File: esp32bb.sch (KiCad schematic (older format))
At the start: 31 parts, among them CON1 Micro_SD_Card, IC1 FT232RQ, J1 CONN_01X18, P1 CONN_01X17, P3 USB_OTG, Q1 MMBT3904, Q2 MMBT3904, SW1 SWITCH_SPST, SW2 SWITCH_SPST, U1 ESP32-WROOM, U2 NJU7223DL1-33

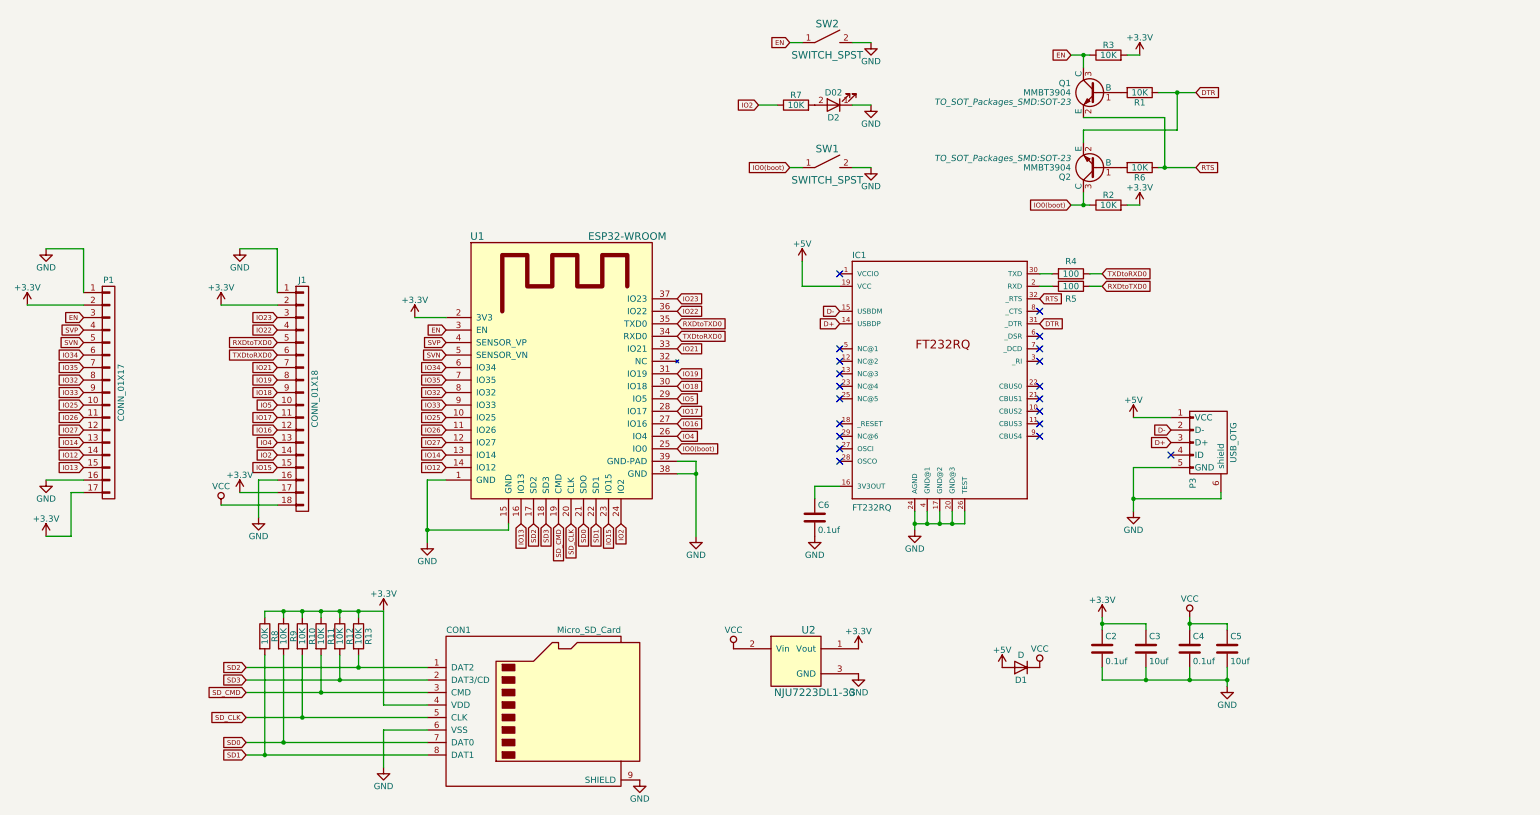
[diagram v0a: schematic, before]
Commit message: Update schema to use CP2102 and NCP1117DT33 and remove SD card holder
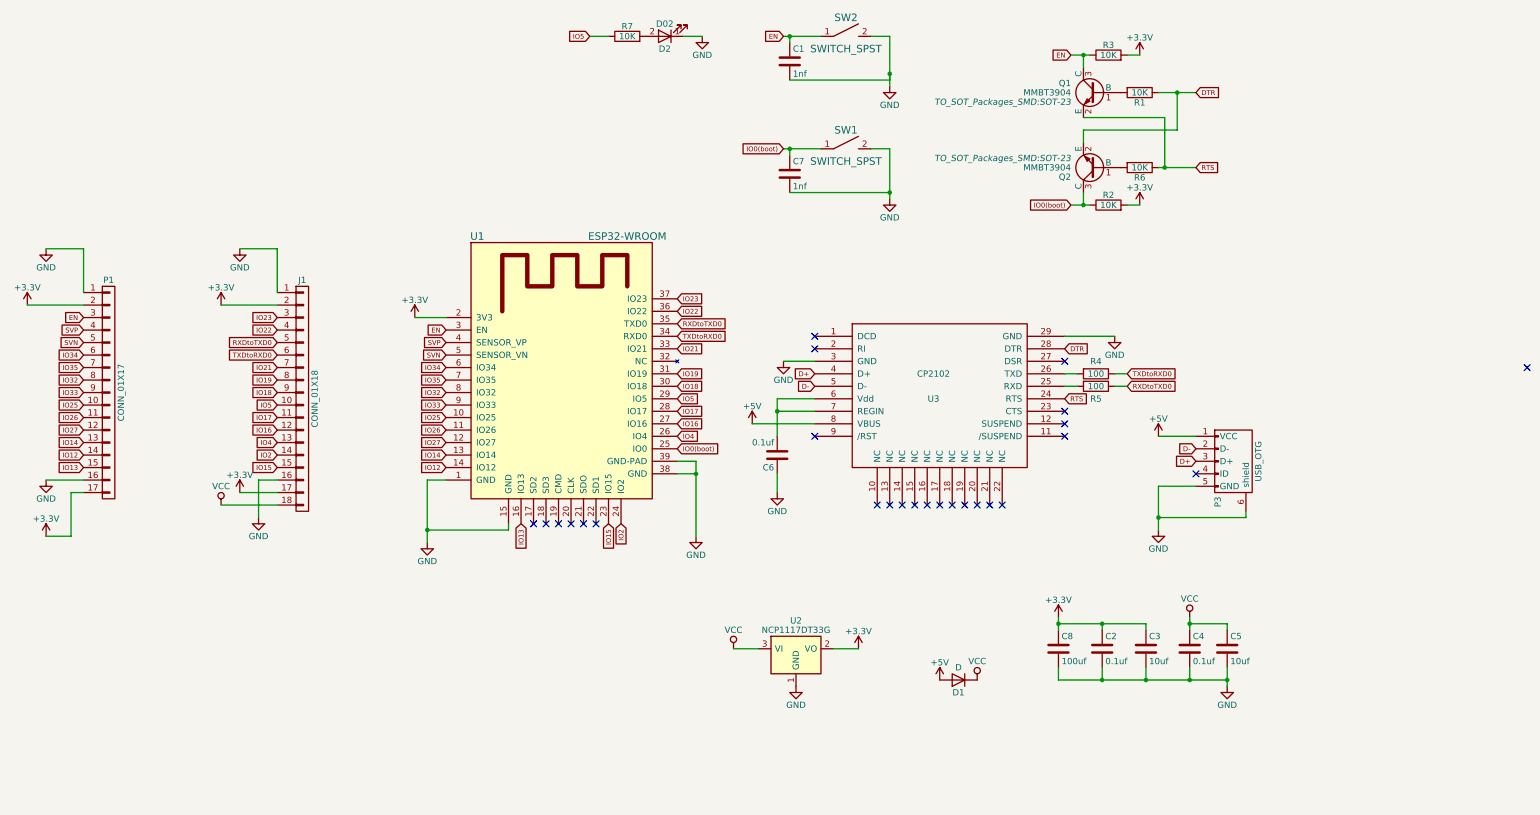
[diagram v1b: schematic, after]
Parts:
- removed CON1: Micro_SD_Card, Connectors_Hirose:microSD_Card_Receptacle_Hirose_DM3AT-SF-PEJM5, symbol Micro_SD_Card
- removed IC1: FT232RQ, ftdi232rq:FR232RQ, symbol FT232RQ
- removed R10, R11, R12, R13, R8, R9: 10K, Resistors_SMD:R_0603, symbol R
- removed U2: NJU7223DL1-33, TO_SOT_Packages_SMD:TO-252-2Lead, symbol NJU7223DL1-33
- added C1, C7: 1nf, Capacitors_SMD:C_0603, symbol C
- added C8: 100uf, Capacitors_SMD:C_1206, symbol C
- added U2: NCP1117DT33G, TO_SOT_Packages_SMD:TO-263-3Lead, symbol NCP1117DT33G
- added U3: CP2102, Housings_DFN_QFN:QFN-28-1EP_5x5mm_Pitch0.5mm, symbol CP2102
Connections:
- net +3V3: now also C8.1, U2.2 (VO)
- net +5V: now also U3.8 (VBUS)
- net D+: now also U3.4 (D+)
- net D-: now also U3.5 (D-)
- net DTR: now also U3.28 (DTR)
- net EN: now also C1.1
- net GND: now also C6.1, C1.2, C7.2, C8.2, U2.1 (GND), U3.29 (GND), U3.3 (GND); no longer C6.2
- net IO0(boot): now also C7.1
- net IO2: no longer R7.1
- net IO5: now also R7.1
- net RTS: now also U3.24 (RTS)
- net VCC: now also U2.3 (VI)
- net at R5.2: now also U3.25 (RXD)
- net at R4.2: now also U3.26 (TXD)
- net SD0: no longer names the net of U1.21 (SDO)
- net SD1: no longer names the net of U1.22 (SD1)
- net SD2: no longer names the net of U1.17 (SD2)
- net SD3: no longer names the net of U1.18 (SD3)
- net SD_CLK: no longer names the net of U1.20 (CLK)
- net SD_CMD: no longer names the net of U1.19 (CMD)
- new net: C6.2, U3.6 (Vdd), U3.7 (REGIN)
- no-connect marks 20 -> 26
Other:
- moved on the sheet: C6, D1, D2, P3, R4, R5, R7, SW1, SW2

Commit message: Update pcb for rev2.0
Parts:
- removed J1: CONN_01X18, common:Pin_Header_Straight_1x18_Pitch2.54mm, symbol CONN_01X18
- removed U2: NCP1117DT33G, TO_SOT_Packages_SMD:TO-263-3Lead, symbol NCP1117DT33G
- added P2: CONN_01X17, common:Pin_Header_Straight_1x17_Pitch2.54mm, symbol CONN_01X17
- added U2: NCP1117ST33T3G, TO_SOT_Packages_SMD:SOT-223, symbol NCP1117ST33T3G
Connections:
- net +3V3: now also P2.17 (P17), P2.2 (P2), U2.2 (VO); no longer P1.17 (P17)
- net GND: now also P2.1 (P1), U2.1 (GND)
- net IO0(boot): now also P2.14 (P14)
- net IO15: now also P2.16 (P16)
- net IO16: now also P2.12 (P12)
- net IO17: now also P2.11 (P11)
- net IO18: now also P2.9 (P9)
- net IO19: now also P2.8 (P8)
- net IO2: now also P2.15 (P15)
- net IO21: now also P2.7 (P7)
- net IO22: now also P2.4 (P4)
- net IO23: now also P2.3 (P3)
- net IO4: now also P2.13 (P13)
- net IO5: now also P2.10 (P10)
- net RXDtoTXD0: now also P2.5 (P5)
- net TXDtoRXD0: now also P2.6 (P6)
- net VCC: now also P1.17 (P17), U2.3 (VI)

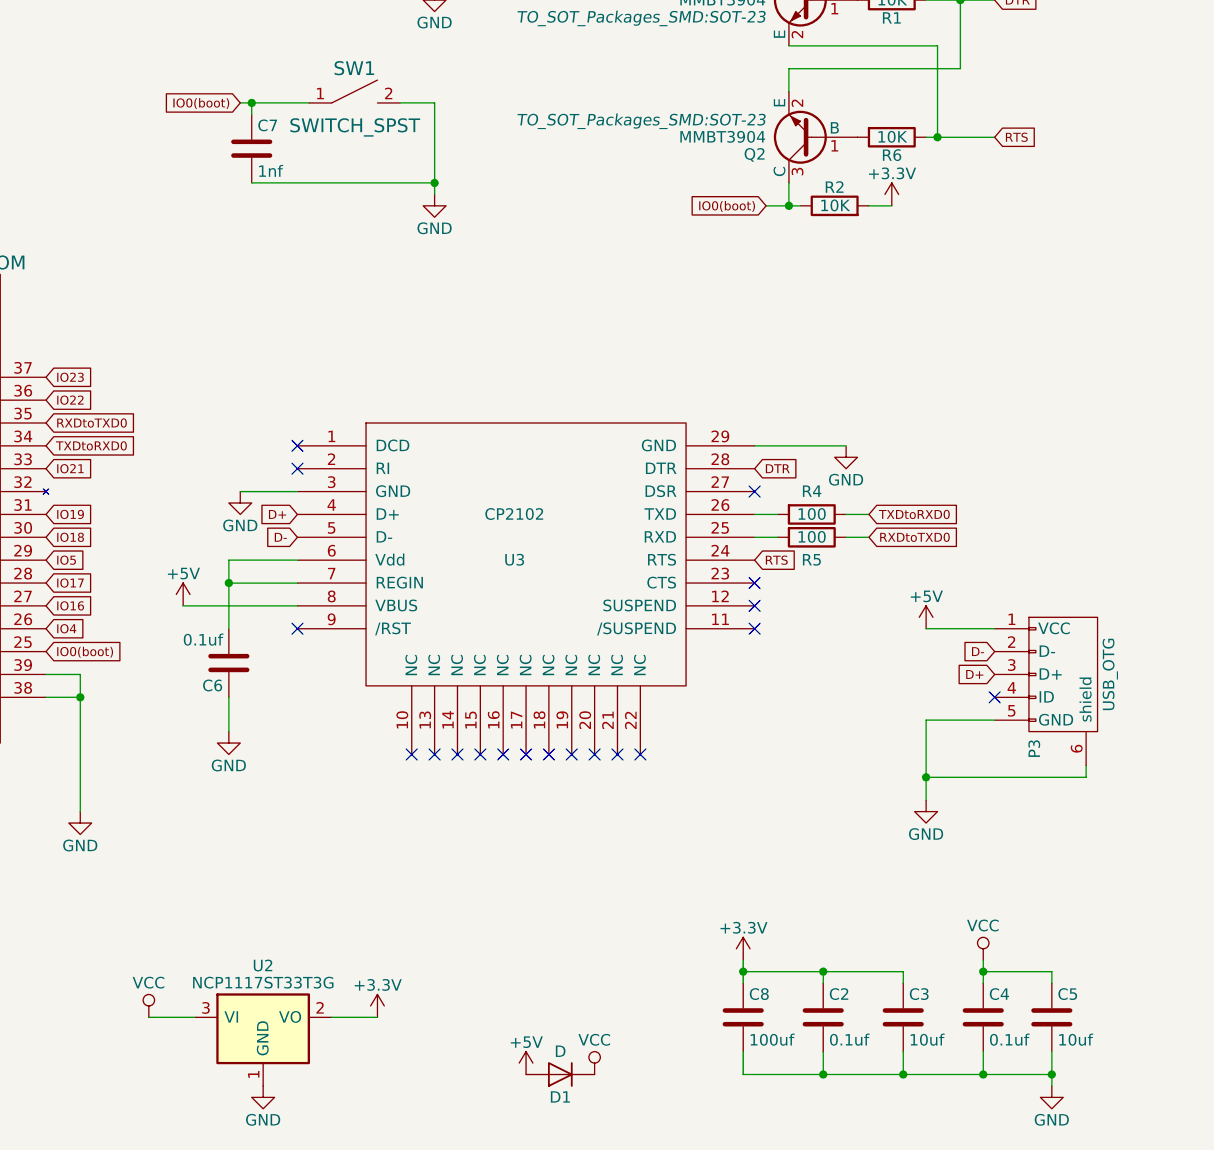
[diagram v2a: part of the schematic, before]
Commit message: Correct and update schema and pcb for rev2.1
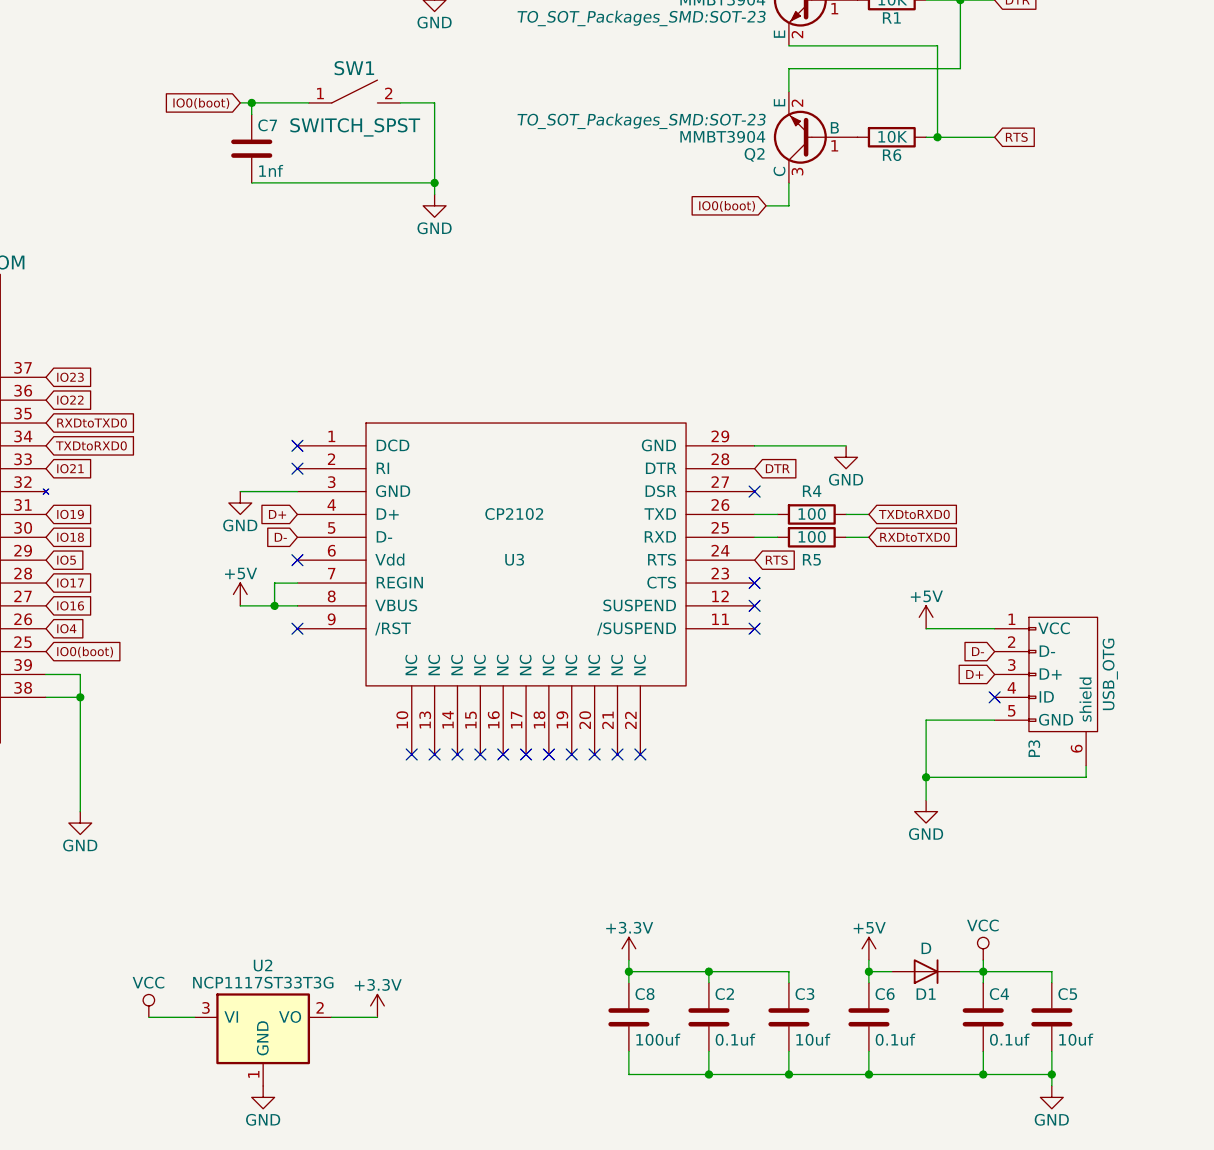
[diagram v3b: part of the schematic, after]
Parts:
- removed R2: 10K, Resistors_SMD:R_0603, symbol R
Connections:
- net +5V: now also C6.1, U3.7 (REGIN)
- net GND: now also C6.2; no longer C6.1
- now unconnected: U3.6 (Vdd)
- no-connect marks 26 -> 27
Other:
- moved on the sheet: C2, C3, C6, C8, D1
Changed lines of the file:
@@
 Sheet 1 1
 Title "ESP32BB"
-Date "2017-03-18"
-Rev "2.0"
+Date "2017-03-28"
+Rev "2.1"
 Comp ""
 Comment1 "by asukiaaa"
@@
 L D D1
 U 1 1 5894AB20
-P 8650 6050
-F 0 "D1" H 8650 6150 50  0000 C CNN
-F 1 "D" H 8650 5950 50  0000 C CNN
-F 2 "Diodes_SMD:D_0805" H 8650 6050 50  0001 C CNN
-F 3 "" H 8650 6050 50  0000 C CNN
-	1    8650 6050
+P 10250 5600
+F 0 "D1" H 10250 5700 50  0000 C CNN
+F 1 "D" H 10250 5500 50  0000 C CNN
+F 2 "Diodes_SMD:D_0805" H 10250 5600 50  0001 C CNN
+F 3 "" H 10250 5600 50  0000 C CNN
+	1    10250 5600
 	-1   0    0    1
-$EndComp
-$Comp
-L VCC #PWR015
-U 1 1 5894AB64
-P 8800 6050
-F 0 "#PWR015" H 8800 5900 50  0001 C CNN
-F 1 "VCC" H 8800 6200 50  0000 C CNN
-F 2 "" H 8800 6050 50  0000 C CNN
-F 3 "" H 8800 6050 50  0000 C CNN
-	1    8800 6050
-	1    0    0    -1
 $EndComp
 $Comp
 L +5V #PWR016
 U 1 1 5894AB9B
-P 8500 6050
-F 0 "#PWR016" H 8500 5900 50  0001 C CNN
-F 1 "+5V" H 8500 6190 50  0000 C CNN
-F 2 "" H 8500 6050 50  0000 C CNN
-F 3 "" H 8500 6050 50  0000 C CNN
-	1    8500 6050
+P 10000 5550
+F 0 "#PWR016" H 10000 5400 50  0001 C CNN
+F 1 "+5V" H 10000 5690 50  0000 C CNN
+F 2 "" H 10000 5550 50  0000 C CNN
+F 3 "" H 10000 5550 50  0000 C CNN
+	1    10000 5550
 	1    0    0    -1
 $EndComp
@@
 L +3.3V #PWR017
 U 1 1 5894AD31
-P 9450 5550
-F 0 "#PWR017" H 9450 5400 50  0001 C CNN
-F 1 "+3.3V" H 9450 5690 50  0000 C CNN
-F 2 "" H 9450 5550 50  0000 C CNN
-F 3 "" H 9450 5550 50  0000 C CNN
-	1    9450 5550
+P 8950 5550
+F 0 "#PWR017" H 8950 5400 50  0001 C CNN
+F 1 "+3.3V" H 8950 5690 50  0000 C CNN
+F 2 "" H 8950 5550 50  0000 C CNN
+F 3 "" H 8950 5550 50  0000 C CNN
+	1    8950 5550
 	1    0    0    -1
 $EndComp
@@
 L C C2
 U 1 1 5894AF56
-P 9800 5800
-F 0 "C2" H 9825 5900 50  0000 L CNN
-F 1 "0.1uf" H 9825 5700 50  0000 L CNN
-F 2 "Capacitors_SMD:C_0603" H 9838 5650 50  0001 C CNN
-F 3 "" H 9800 5800 50  0000 C CNN
-	1    9800 5800
+P 9300 5800
+F 0 "C2" H 9325 5900 50  0000 L CNN
+F 1 "0.1uf" H 9325 5700 50  0000 L CNN
+F 2 "Capacitors_SMD:C_0603" H 9338 5650 50  0001 C CNN
+F 3 "" H 9300 5800 50  0000 C CNN
+	1    9300 5800
 	1    0    0    -1
 $EndComp
@@
 L C C3
 U 1 1 5894B158
-P 10150 5800
-F 0 "C3" H 10175 5900 50  0000 L CNN
-F 1 "10uf" H 10175 5700 50  0000 L CNN
-F 2 "Capacitors_SMD:C_0603" H 10188 5650 50  0001 C CNN
-F 3 "" H 10150 5800 50  0000 C CNN
-	1    10150 5800
+P 9650 5800
+F 0 "C3" H 9675 5900 50  0000 L CNN
+F 1 "10uf" H 9675 5700 50  0000 L CNN
+F 2 "Capacitors_SMD:C_0603" H 9688 5650 50  0001 C CNN
+F 3 "" H 9650 5800 50  0000 C CNN
+	1    9650 5800
 	1    0    0    -1
 $EndComp
@@
 L C C6
 U 1 1 589879F3
-P 7200 4250
-F 0 "C6" H 7225 4350 50  0000 L CNN
-F 1 "0.1uf" H 7225 4150 50  0000 L CNN
-F 2 "Capacitors_SMD:C_0603" H 7238 4100 50  0001 C CNN
-F 3 "" H 7200 4250 50  0000 C CNN
-	1    7200 4250
-	-1   0    0    1
-$EndComp
-$Comp
-L GND #PWR021
-U 1 1 58987AAB
-P 7200 4550
-F 0 "#PWR021" H 7200 4300 50  0001 C CNN
-F 1 "GND" H 7200 4400 50  0000 C CNN
-F 2 "" H 7200 4550 50  0000 C CNN
-F 3 "" H 7200 4550 50  0000 C CNN
-	1    7200 4550
+P 10000 5800
+F 0 "C6" H 10025 5900 50  0000 L CNN
+F 1 "0.1uf" H 10025 5700 50  0000 L CNN
+F 2 "Capacitors_SMD:C_0603" H 10038 5650 50  0001 C CNN
+F 3 "" H 10000 5800 50  0000 C CNN
+	1    10000 5800
 	1    0    0    -1
 $EndComp
@@
 L +5V #PWR022
 U 1 1 58A84984
-P 7000 4000
-F 0 "#PWR022" H 7000 3850 50  0001 C CNN
-F 1 "+5V" H 7000 4140 50  0000 C CNN
-F 2 "" H 7000 4000 50  0000 C CNN
-F 3 "" H 7000 4000 50  0000 C CNN
-	1    7000 4000
+P 7250 4000
+F 0 "#PWR022" H 7250 3850 50  0001 C CNN
+F 1 "+5V" H 7250 4140 50  0000 C CNN
+F 2 "" H 7250 4000 50  0000 C CNN
+F 3 "" H 7250 4000 50  0000 C CNN
+	1    7250 4000
 	1    0    0    -1
 $EndComp
@@
 $EndComp
 $Comp
-L R R2
-U 1 1 58A9CA4D
-P 9850 2250
-F 0 "R2" V 9930 2250 50  0000 C CNN
-F 1 "10K" V 9850 2250 50  0000 C CNN
-F 2 "Resistors_SMD:R_0603" V 9780 2250 50  0001 C CNN
-F 3 "" H 9850 2250 50  0000 C CNN
-	1    9850 2250
-	0    -1   -1   0
-$EndComp
-$Comp
-L +3.3V #PWR024
-U 1 1 58A9CA53
-P 10100 2250
-F 0 "#PWR024" H 10100 2100 50  0001 C CNN
-F 1 "+3.3V" H 10100 2390 50  0000 C CNN
-F 2 "" H 10100 2250 50  0000 C CNN
-F 3 "" H 10100 2250 50  0000 C CNN
-	1    10100 2250
-	1    0    0    -1
-$EndComp
-$Comp
 L SWITCH_SPST SW1
 U 1 1 58AADA65
@@
 L C C8
 U 1 1 58CD61C2
-P 9450 5800
-F 0 "C8" H 9475 5900 50  0000 L CNN
-F 1 "100uf" H 9475 5700 50  0000 L CNN
-F 2 "Capacitors_SMD:C_1206" H 9488 5650 50  0001 C CNN
-F 3 "" H 9450 5800 50  0000 C CNN
-	1    9450 5800
+P 8950 5800
+F 0 "C8" H 8975 5900 50  0000 L CNN
+F 1 "100uf" H 8975 5700 50  0000 L CNN
+F 2 "Capacitors_SMD:C_1206" H 8988 5650 50  0001 C CNN
+F 3 "" H 8950 5800 50  0000 C CNN
+	1    8950 5800
 	1    0    0    -1
 $EndComp
@@
 	1350 4450 1650 4450
 Wire Wire Line
-	10150 5600 10150 5650
+	9650 5600 9650 5650
 Wire Wire Line
 	10500 5550 10500 5650
 Wire Wire Line
-	10500 5600 10800 5600
+	10400 5600 10800 5600
 Wire Wire Line
 	10800 5600 10800 5650
@@
 Connection ~ 10500 6050
 Wire Wire Line
-	10150 6050 10150 5950
-Connection ~ 10150 6050
+	9650 6050 9650 5950
+Connection ~ 9650 6050
 Wire Wire Line
 	10250 4500 10250 4850
@@
 	1550 4900 1350 4900
 Wire Wire Line
-	9800 5950 9800 6050
-Wire Wire Line
-	9450 6050 10800 6050
+	9300 5950 9300 6050
 Wire Wire Line
 	9500 3600 9600 3600
@@
 Wire Wire Line
 	9650 1050 9650 1150
-Wire Wire Line
-	9550 2250 9700 2250
 Wire Wire Line
 	9650 2250 9650 2150
@@
 Wire Wire Line
 	10000 1050 10100 1050
-Connection ~ 9650 2250
-Wire Wire Line
-	10000 2250 10100 2250
 Wire Wire Line
 	5700 900  5850 900
@@
 Connection ~ 8100 2150
 Wire Wire Line
-	9450 5550 9450 5650
-Wire Wire Line
-	9450 5600 10150 5600
-Connection ~ 9450 5600
-Wire Wire Line
-	9800 5650 9800 5600
-Connection ~ 9800 5600
-Wire Wire Line
-	9450 5950 9450 6050
-Connection ~ 9800 6050
+	8950 5550 8950 5650
+Wire Wire Line
+	8950 5600 9650 5600
+Connection ~ 8950 5600
+Wire Wire Line
+	9300 5650 9300 5600
+Connection ~ 9300 5600
+Wire Wire Line
+	8950 5950 8950 6050
+Connection ~ 9300 6050
 Wire Wire Line
 	6850 5800 7050 5800
@@
 	7650 5800 7850 5800
 Wire Wire Line
-	7200 3800 7200 4100
-Wire Wire Line
-	7200 4400 7200 4550
-Wire Wire Line
 	9500 3300 9900 3300
 Wire Wire Line
 	7250 3500 7500 3500
 Wire Wire Line
-	7000 4000 7500 4000
-Wire Wire Line
-	7200 3900 7500 3900
-Wire Wire Line
-	7500 3800 7200 3800
-Connection ~ 7200 3900
-Wire Wire Line
 	2750 4550 3200 4550
+Wire Wire Line
+	9550 2250 9650 2250
+NoConn ~ 7500 3800
+Wire Wire Line
+	7250 4000 7500 4000
+Wire Wire Line
+	7500 3900 7400 3900
+Wire Wire Line
+	7400 3900 7400 4000
+Connection ~ 7400 4000
+Wire Wire Line
+	10000 5550 10000 5650
+Wire Wire Line
+	8950 6050 10800 6050
+Wire Wire Line
+	10000 5600 10100 5600
+Connection ~ 10000 5600
+Wire Wire Line
+	10000 5950 10000 6050
+Connection ~ 10000 6050
 $EndSCHEMATC

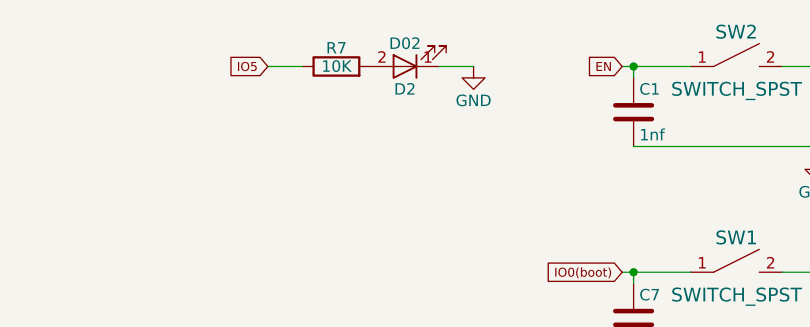
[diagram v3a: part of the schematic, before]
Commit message: Correct label of led on schema
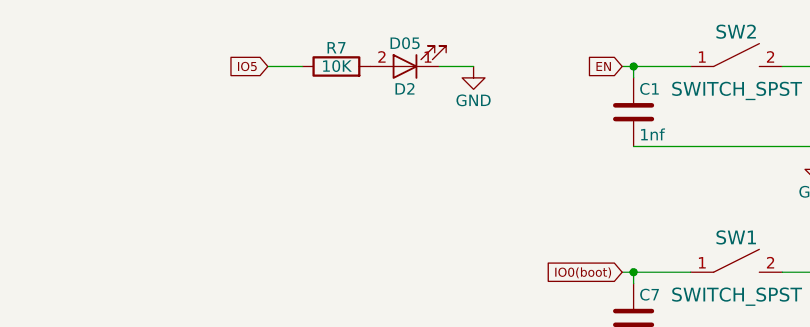
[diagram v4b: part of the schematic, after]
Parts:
- D2: value D02 -> D05
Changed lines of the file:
@@
 P 6300 900
 F 0 "D2" H 6300 1000 50  0000 C CNN
-F 1 "D02" H 6300 800 50  0000 C CNN
+F 1 "D05" H 6300 800 50  0000 C CNN
 F 2 "LEDs:LED_0603" H 6300 900 50  0001 C CNN
 F 3 "" H 6300 900 50  0000 C CNN
